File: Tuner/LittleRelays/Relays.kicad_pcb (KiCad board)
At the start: 2 copper layers, 100 x 100 mm, 86 parts, among them J1 Conn_01x03, J10 Conn_01x02, J11 Conn_01x02, J12 Conn_01x01, J13 Conn_01x01, J14 Conn_01x01, J15 Conn_01x01, J16 Conn_01x02, J17 Conn_02x10_Odd_Even, J18 Conn_01x02, J19 Conn_01x03, J2 Conn_01x03, J3 Conn_01x03, J4 Conn_01x03, J5 Conn_01x03, J6 Conn_01x03, J7 Conn_01x03, J8 Conn_01x02, J9 Conn_01x02

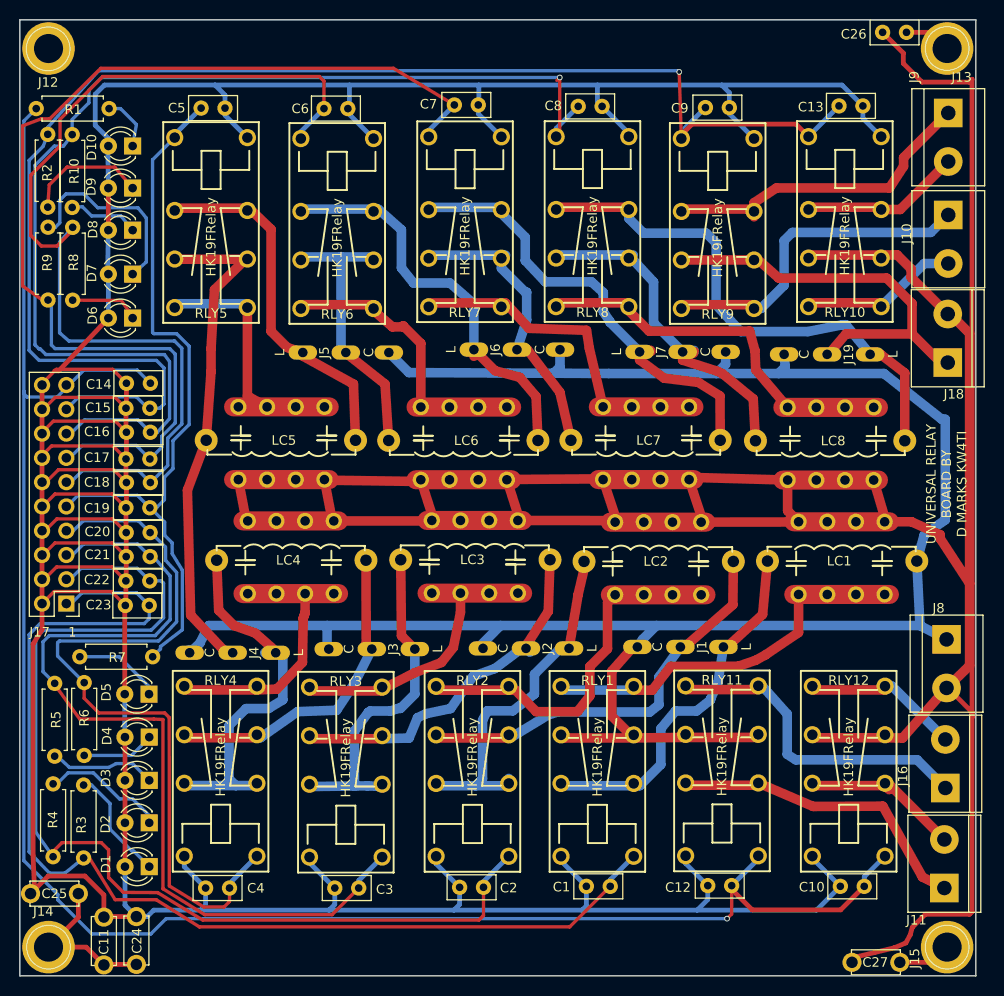
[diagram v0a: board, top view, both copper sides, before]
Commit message: Error in pinout HK19F fixed
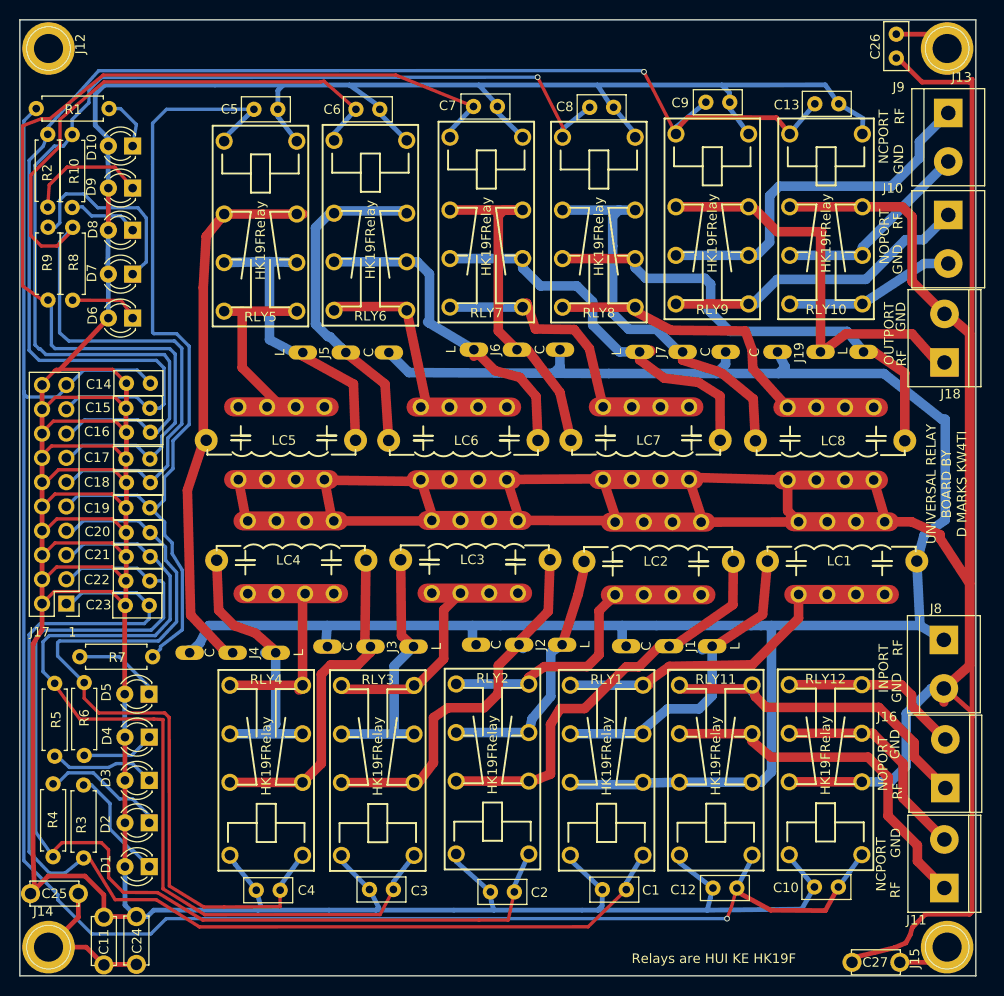
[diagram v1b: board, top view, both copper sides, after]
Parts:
- moved C5 5.53 mm to (74.5, 59.4)
- moved C4 5.30 mm to (77.2, 141.0)
- moved RLY5 5.18 mm to (75.2, 65.1)
- moved RLY4 4.77 mm to (75.8, 135.0)
- moved C3 3.64 mm to (89.1, 141.0)
- moved RLY6 3.47 mm to (86.7, 65.0)
- moved RLY3 3.35 mm to (87.4, 135.0)
- moved C6 3.34 mm to (85.2, 59.4)
- moved C2 3.26 mm to (101.7, 141.2)
- moved C10 2.71 mm to (135.6, 140.7)
- moved C13 2.53 mm to (133.2, 58.8)
- moved RLY12 2.42 mm to (134.3, 135.0)
- moved RLY7 2.23 mm to (98.8, 64.7)
- moved RLY2 2.11 mm to (99.4, 134.9)
- moved C7 2.01 mm to (97.5, 59.1)
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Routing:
- net RFGND: track 322.1 -> 335.5 mm
- net RLY5: track 78.9 -> 91.1 mm
- net Net-(J2-Pad1): track 39.4 -> 28.9 mm
- net Net-(J4-Pad1): track 40.7 -> 31.6 mm
- net Net-(J3-Pad1): track 36.0 -> 27.9 mm
- net Net-(J6-Pad1): track 43.6 -> 35.9 mm
- net Net-(J5-Pad2): track 29.9 -> 37.2 mm
- net Net-(J11-Pad1): track 32.2 -> 38.4 mm
- net Net-(J11-Pad2): track 16.9 -> 22.9 mm
- net Net-(J7-Pad2): track 35.6 -> 41.7 mm
- net Net-(J5-Pad1): track 38.3 -> 32.3 mm
- net Net-(J6-Pad2): track 32.0 -> 37.8 mm
- net Net-(J7-Pad1): track 48.3 -> 42.9 mm
- net RLY4: track 81.1 -> 86.3 mm
- net Net-(J19-Pad1): track 55.8 -> 50.6 mm
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
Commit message: JLCPCB Nov 1 2018
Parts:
- removed C26: 10 nF, Capacitors_THT:C_Disc_D5.0mm_W2.5mm_P2.50mm
- removed C27: 10 nF, Capacitors_THT:C_Disc_D5.0mm_W2.5mm_P5.00mm
- added J20: Conn_01x01, tuner:SOLDERJUMPER, F.Cu at (129.9, 123.2)
- added J21: Conn_01x01, tuner:SOLDERJUMPER, F.Cu at (130.2, 116.5)
- added J22: Conn_01x01, tuner:SOLDERJUMPER, F.Cu at (137.2, 115.6)
- added J23: Conn_01x01, tuner:SOLDERJUMPER, F.Cu at (129.7, 75.4)
- added J24: Conn_01x01, tuner:SOLDERJUMPER, F.Cu at (129.7, 80.9)
- added J25: Conn_01x01, tuner:SOLDERJUMPER, F.Cu at (141.6, 52.0)
- added J26: Conn_01x01, tuner:SOLDERJUMPER, F.Cu at (138.5, 52.0)
- added J27: Conn_01x01, tuner:SOLDERJUMPER, F.Cu at (137.4, 147.0)
- added J28: Conn_01x01, tuner:SOLDERJUMPER, F.Cu at (140.3, 146.9)
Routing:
- net RFGND: track 335.5 -> 229.9 mm
- net Net-(J15-Pad1): track 5.92 -> 11.0 mm
- net Net-(J13-Pad1): track 9.81 -> 13.7 mm
- net Net-(J16-Pad2): track 19.3 -> 22.8 mm
- net Net-(J11-Pad2): track 22.9 -> 25.7 mm
- net Net-(J10-Pad2): track 17.8 -> 20.5 mm
- net Net-(J23-Pad1): track 21.1 -> 23.6 mm
- net Net-(J9-Pad1): track 38.5 -> 37.8 mm
- net RFSIG: track 220.3 -> 219.7 mm
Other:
- board text added: "NCGND"
- board text added: "NOGND"
- board text added: "Relays are HUI KE HK19F Hongfa HDF2 Omron G5RV-2"
- board text removed: "Relays are HUI KE HK19F"

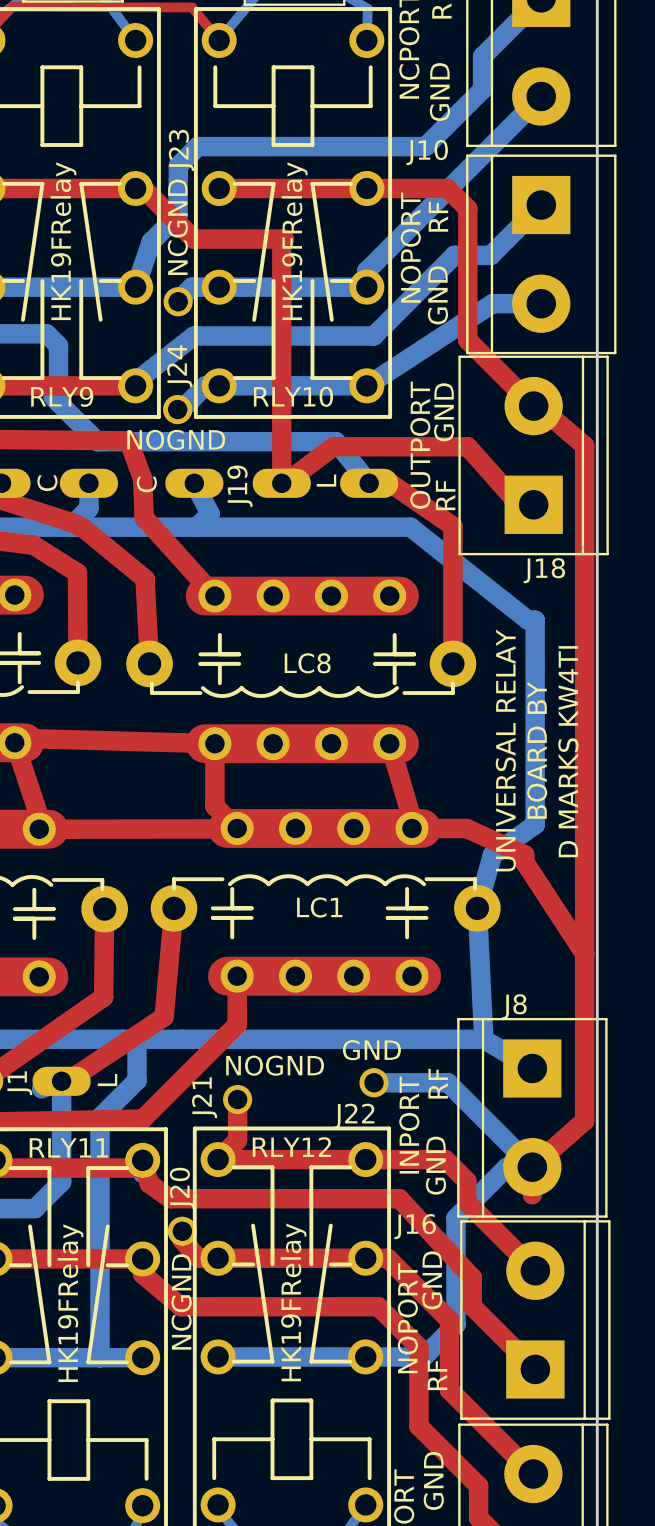
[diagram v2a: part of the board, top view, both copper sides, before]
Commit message: Moved some grounds around
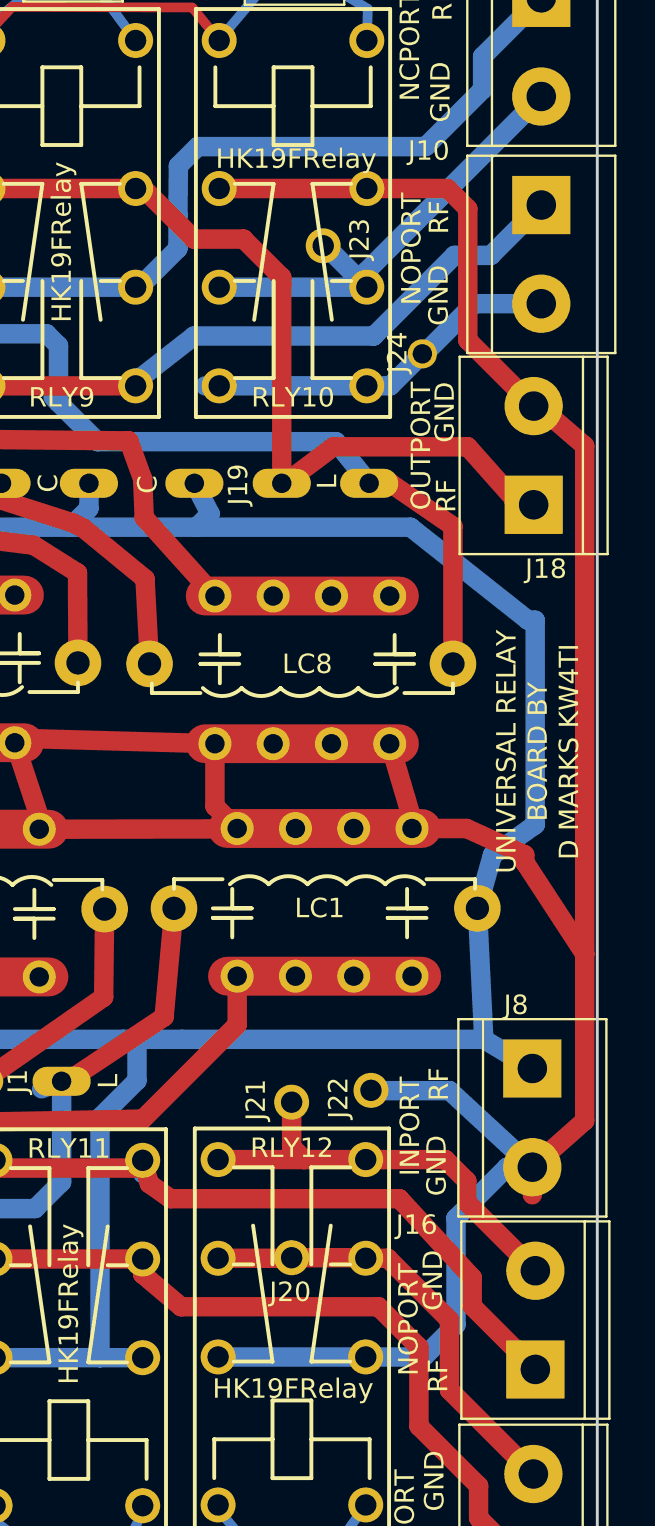
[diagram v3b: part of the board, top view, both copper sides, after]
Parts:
- moved J24 12.9 mm to (142.3, 78.1)
- moved J23 8.00 mm to (137.2, 72.5)
- moved J20 5.79 mm to (135.5, 124.6)
- moved J21 2.78 mm to (133.0, 116.6)
- moved J22 0.42 mm to (137.1, 116.0)
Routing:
- net Net-(J11-Pad2): track 25.7 -> 23.0 mm
- net Net-(J10-Pad2): track 20.5 -> 19.0 mm
- net Net-(J18-Pad1): track 44.4 -> 43.1 mm
- net Net-(J23-Pad1): track 23.6 -> 24.3 mm

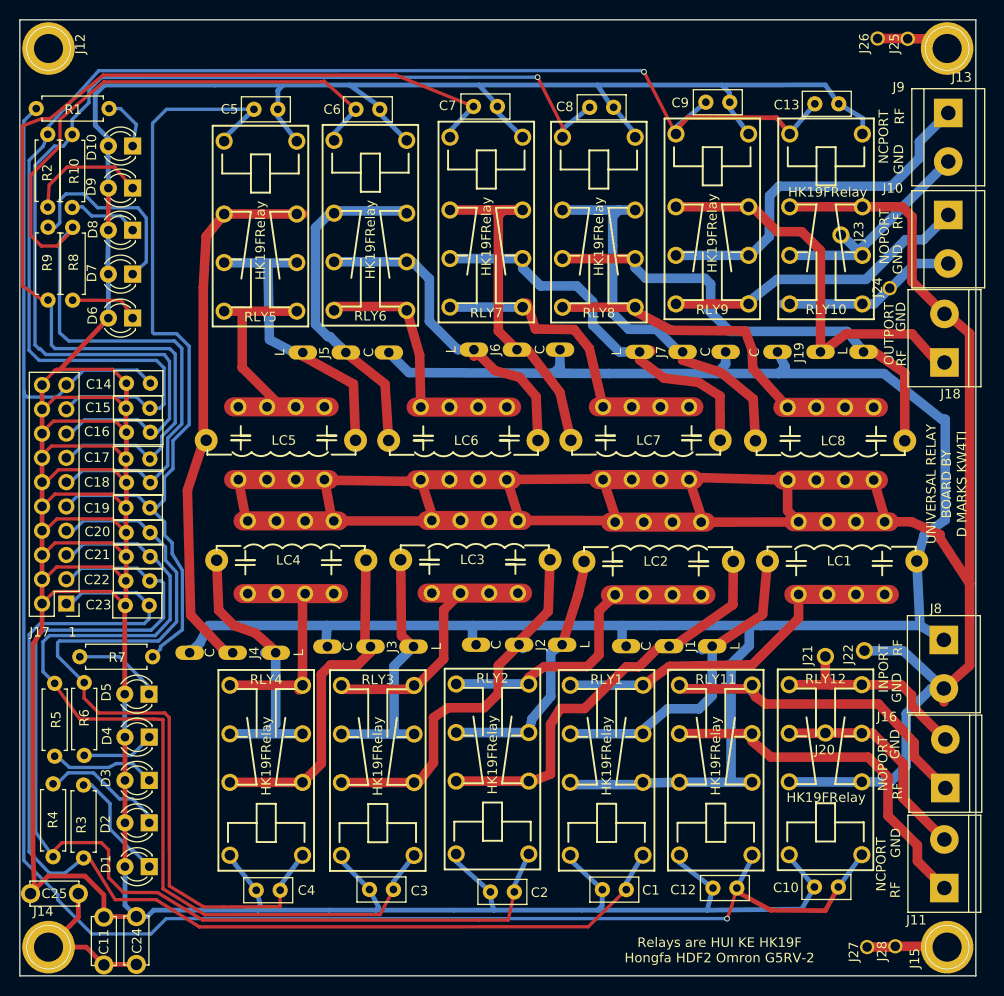
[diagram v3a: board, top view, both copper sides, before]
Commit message: Added extra capacitors between relay power and ground posts
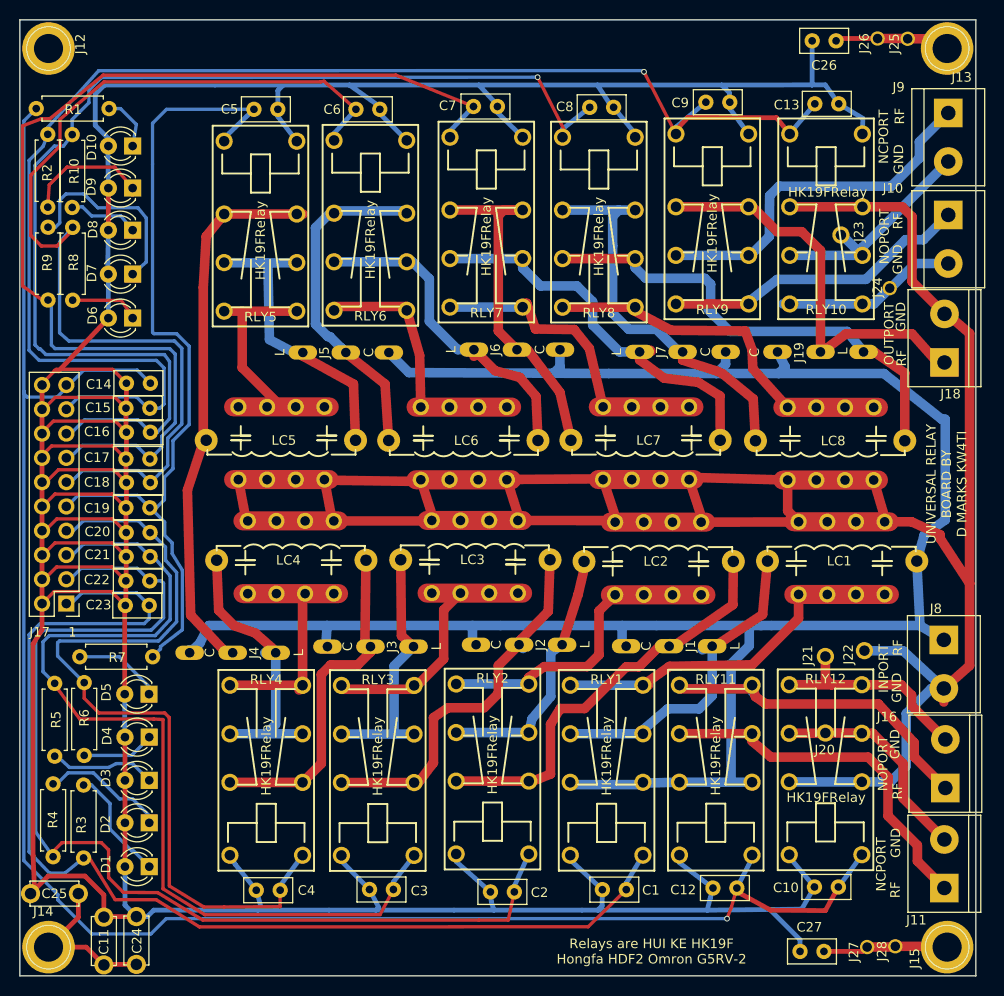
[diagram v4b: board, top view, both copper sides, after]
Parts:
- added C26: 10 nF, Capacitors_THT:C_Disc_D5.0mm_W2.5mm_P2.50mm, F.Cu at (135.4, 52.2)
- added C27: 10 nF, Capacitors_THT:C_Disc_D5.0mm_W2.5mm_P2.50mm, F.Cu at (134.1, 147.4)
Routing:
- net +5V: track 491.6 -> 502.0 mm
- net Net-(C27-Pad1): track 11.0 -> 15.7 mm
- net Net-(C26-Pad1): track 13.7 -> 18.1 mm

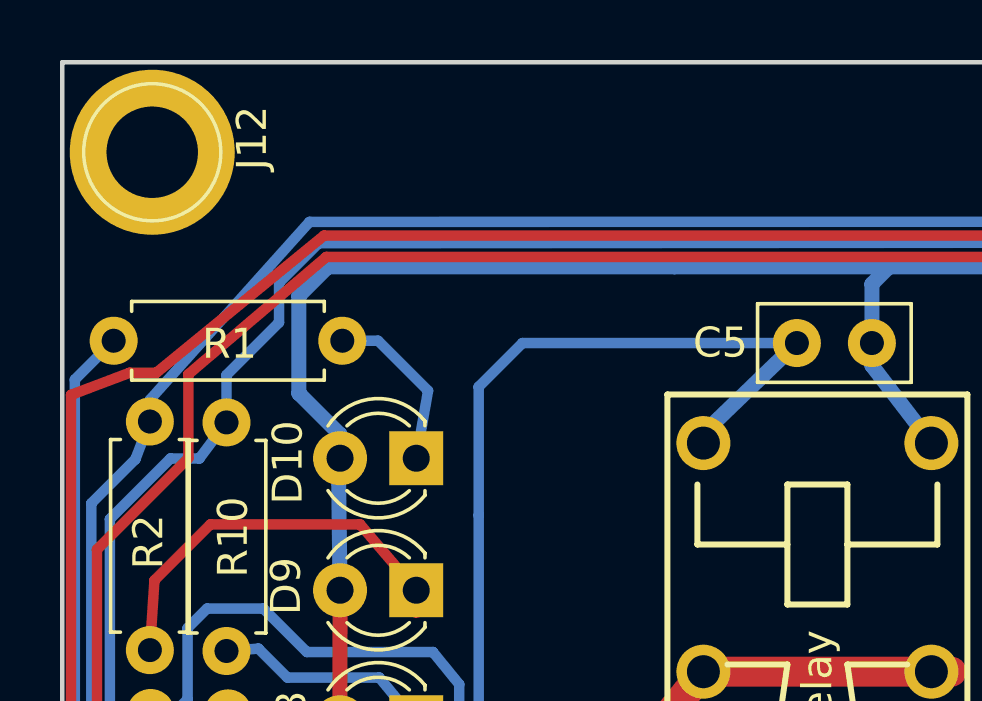
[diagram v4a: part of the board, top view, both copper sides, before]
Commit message: Added extra capacitors to ground to large relay boards
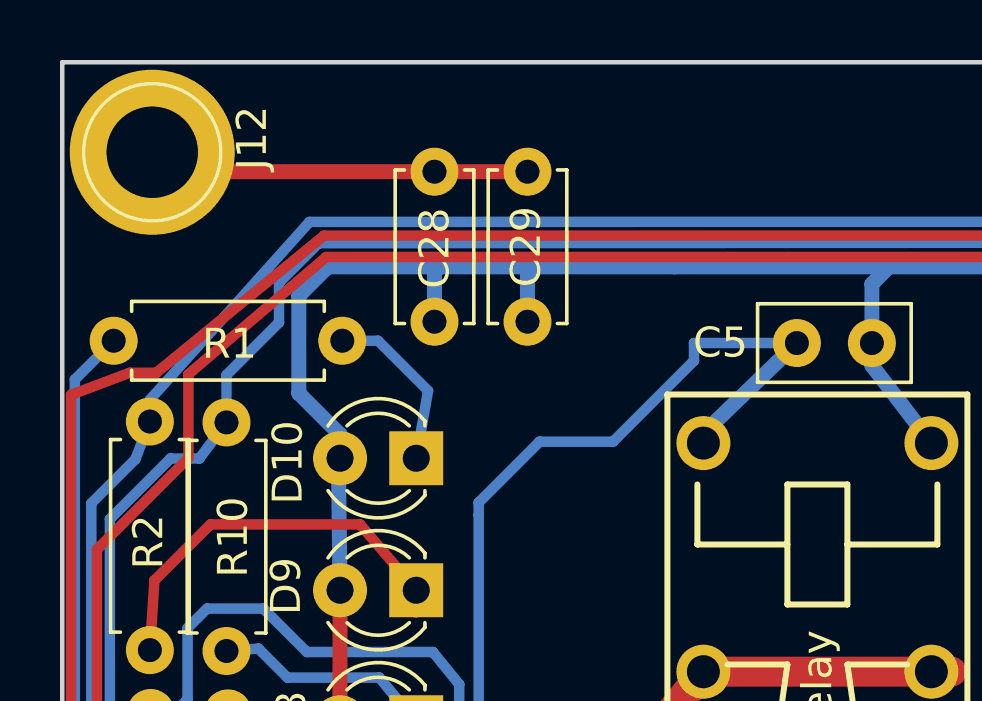
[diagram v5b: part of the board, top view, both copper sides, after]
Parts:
- added C28: 10 nF, Capacitors_THT:C_Disc_D5.0mm_W2.5mm_P5.00mm, F.Cu at (62.4, 53.6)
- added C29: 10 nF, Capacitors_THT:C_Disc_D5.0mm_W2.5mm_P5.00mm, F.Cu at (65.5, 53.6)
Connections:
- J12 pad 1: (no net) -> Net-(C28-Pad1)
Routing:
- net Net-(C28-Pad1): track 0.00 -> 12.8 mm
- net +5V: track 502.0 -> 506.2 mm
- net RLY5: track 91.1 -> 89.2 mm
